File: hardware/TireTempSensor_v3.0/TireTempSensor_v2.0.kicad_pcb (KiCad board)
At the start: 4 copper layers, 75 x 20.5 mm, 75 parts, among them IC2 MLX90621ESF-BAB-000-SP, IC4 TPS54202HDDCR, J2 Main connector, J3 FTSH-107-01-L-D-K, T10 TP_+5V, T14 TP_+3.3V, T15 TP_+2.6V, U1 STM32G0C1KCTxN, U2 MIC5306-2.6YD5-TR, U3 NCP715SQ33T2G, U7 ADM3057ExRW, Y1 ATX-11-F-32.000MHZ-F05-T

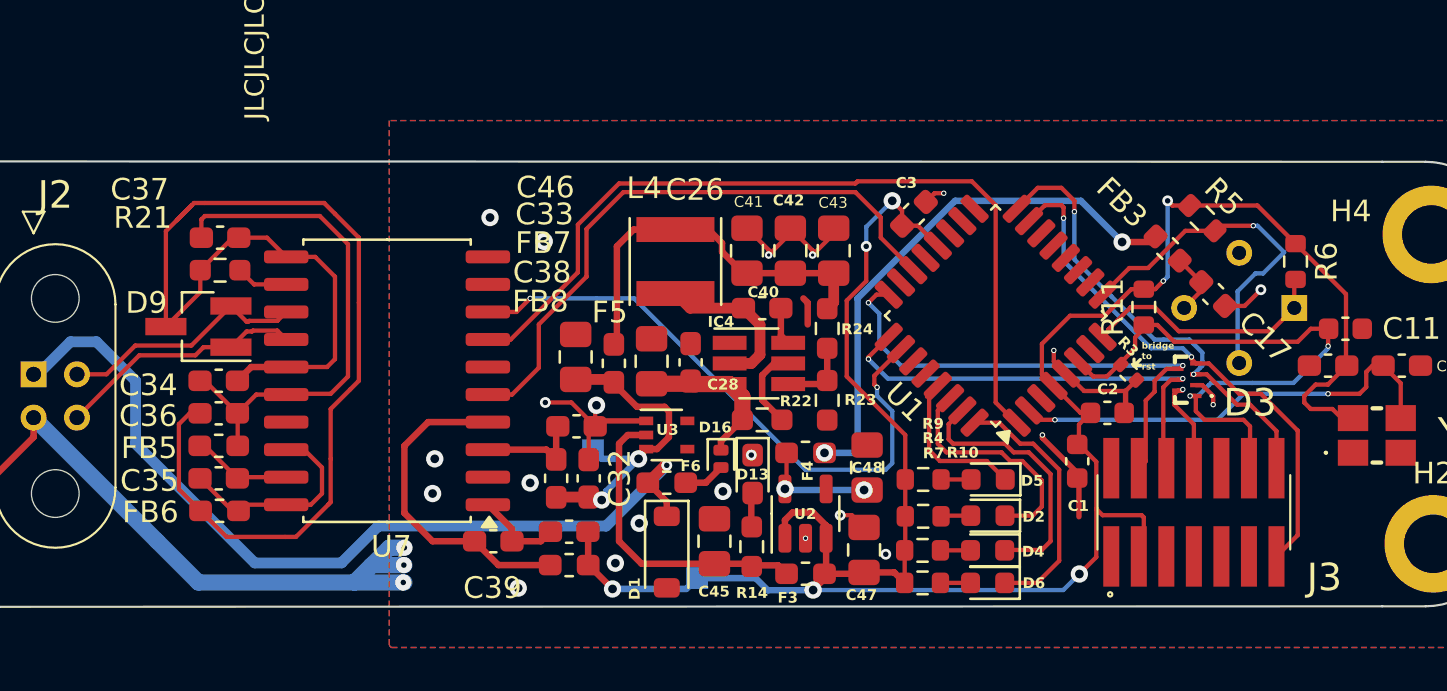
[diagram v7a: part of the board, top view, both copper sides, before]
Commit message: Poprawiono SPI NA I2C
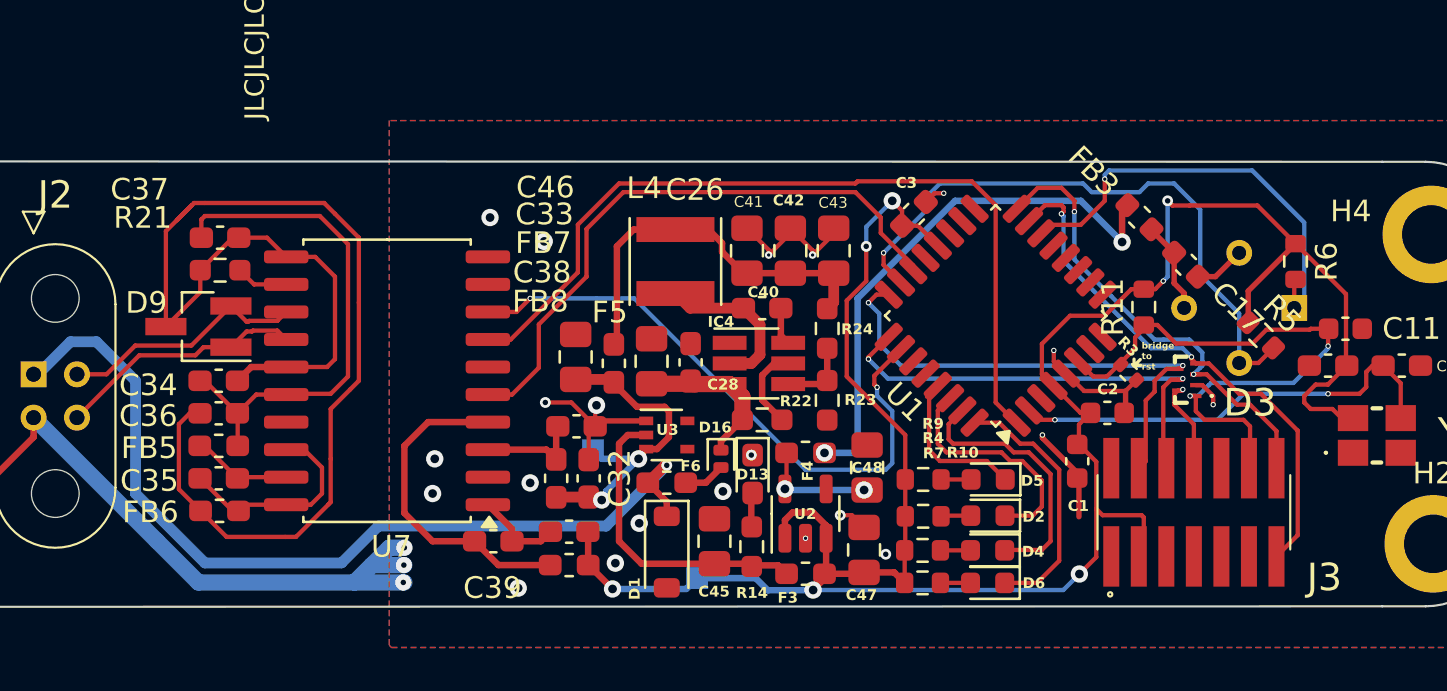
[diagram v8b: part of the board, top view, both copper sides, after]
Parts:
- moved R5 6.04 mm to (159.4, 97.0)
- moved FB3 1.94 mm to (153.8, 91.6)
- moved C17 1.84 mm to (155.9, 93.7)
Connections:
- U1 pad 14: unconnected-(U1-PA7-Pad14) -> /SCL
- U1 pad 23: unconnected-(U1-PA12/PA10-Pad23) -> /SDA
- U1 pad 8: /SCL -> unconnected-(U1-PA1-Pad8)
- U1 pad 9: /SDA -> unconnected-(U1-PA2-Pad9)
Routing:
- net /SDA: track 16.5 -> 28.6 mm
- net /SCL: track 11.7 -> 20.5 mm, vias 0 -> 1
- net +3V3: track 104.9 -> 109.5 mm
- net +24V: track 40.7 -> 42.1 mm
- net Net-(IC2-VDD): track 2.92 -> 4.25 mm
- net GND: track 82.8 -> 82.0 mm, vias 25 -> 24
